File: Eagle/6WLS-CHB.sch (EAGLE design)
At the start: 26 parts, among them U1 DCDCCHB7505, U2 DCDCCHB7515, U3 DCDCCHB7515

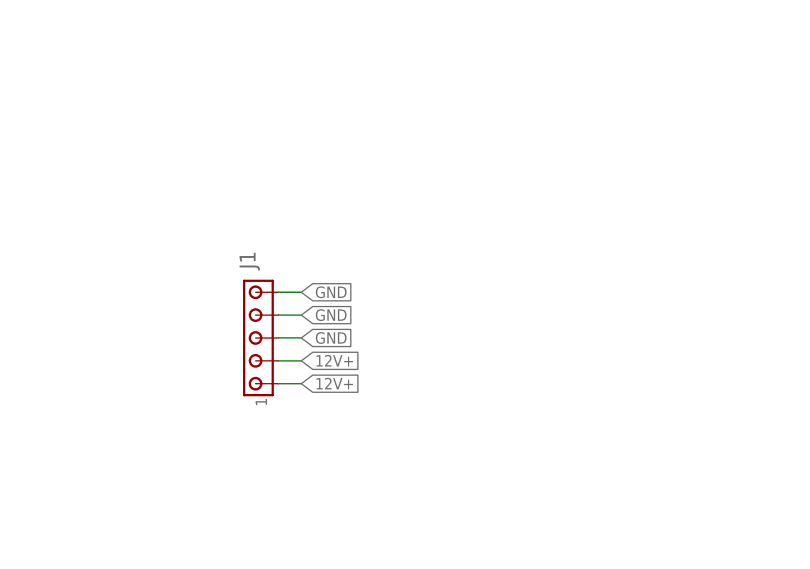
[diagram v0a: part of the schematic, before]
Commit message: Bigger terminal block.
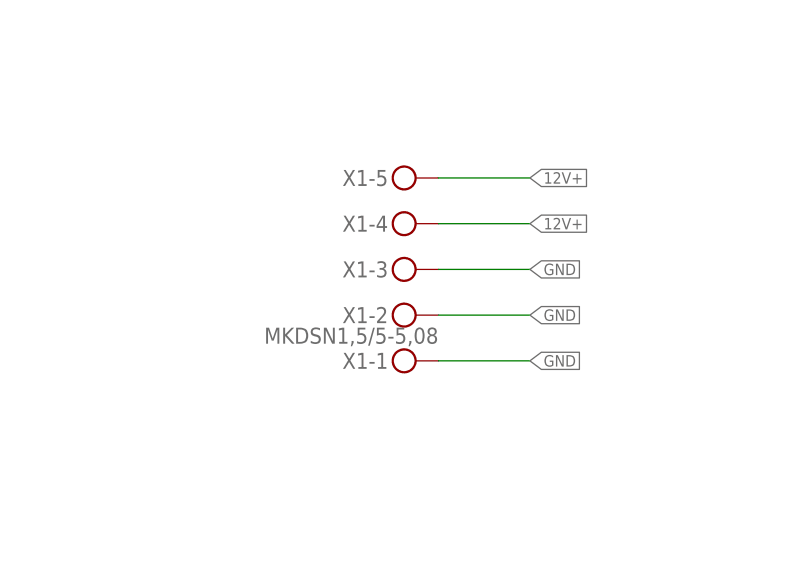
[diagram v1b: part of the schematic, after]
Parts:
- removed J1: (no value), con-amp:MTA05-156
- added X1: MKDSN1,5/5-5,08, con-phoenix-508:MKDSN1,5/5-5,08
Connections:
- net 12V+: now also X1-4.KL, X1-5.KL
- net GND: now also X1-1.KL, X1-2.KL, X1-3.KL
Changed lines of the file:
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@@
 <part name="U3" library="studio_h" deviceset="DCDC" device="CHB7515" value="DCDCCHB7515"/>
 <part name="H15" library="holes" deviceset="MOUNT-PAD-ROUND" device="3.3"/>
-<part name="J1" library="con-amp" deviceset="MTA05-156" device=""/>
+<part name="X1" library="con-phoenix-508" deviceset="MKDSN1,5/5-5,08" device=""/>
 </parts>
 <sheets>
@@
 <instance part="U3" gate="G$1" x="93.98" y="71.12"/>
 <instance part="H15" gate="G$1" x="274.32" y="93.98"/>
-<instance part="J1" gate="G$1" x="58.42" y="195.58" rot="R90"/>
+<instance part="X1" gate="-1" x="76.2" y="198.12" rot="R180"/>
+<instance part="X1" gate="-2" x="76.2" y="203.2" rot="R180"/>
+<instance part="X1" gate="-3" x="76.2" y="208.28" rot="R180"/>
+<instance part="X1" gate="-4" x="76.2" y="213.36" rot="R180"/>
+<instance part="X1" gate="-5" x="76.2" y="218.44" rot="R180"/>
 </instances>
 <busses>
@@
 </segment>
 <segment>
-<wire x1="60.96" y1="198.12" x2="63.5" y2="198.12" width="0.1524" layer="91"/>
-<label x="63.5" y="195.58" size="1.27" layer="95" font="vector" ratio="12" xref="yes"/>
-<label x="63.5" y="198.12" size="1.27" layer="95" font="vector" ratio="12" xref="yes"/>
-</segment>
-<segment>
-<wire x1="60.96" y1="195.58" x2="63.5" y2="195.58" width="0.1524" layer="91"/>
+<wire x1="78.74" y1="218.44" x2="88.9" y2="218.44" width="0.1524" layer="91"/>
+<label x="88.9" y="218.44" size="1.27" layer="95" font="vector" ratio="12" xref="yes"/>
+<pinref part="X1" gate="-5" pin="KL"/>
+</segment>
+<segment>
+<wire x1="78.74" y1="213.36" x2="88.9" y2="213.36" width="0.1524" layer="91"/>
+<label x="88.9" y="213.36" size="1.27" layer="95" font="vector" ratio="12" xref="yes"/>
+<pinref part="X1" gate="-4" pin="KL"/>
 </segment>
 </net>
@@
 </segment>
 <segment>
-<wire x1="60.96" y1="200.66" x2="63.5" y2="200.66" width="0.1524" layer="91"/>
-<label x="63.5" y="200.66" size="1.27" layer="95" font="vector" ratio="12" xref="yes"/>
-</segment>
-<segment>
-<wire x1="60.96" y1="203.2" x2="63.5" y2="203.2" width="0.1524" layer="91"/>
-<label x="63.5" y="203.2" size="1.27" layer="95" font="vector" ratio="12" xref="yes"/>
-</segment>
-<segment>
-<wire x1="60.96" y1="205.74" x2="63.5" y2="205.74" width="0.1524" layer="91"/>
-<label x="63.5" y="205.74" size="1.27" layer="95" font="vector" ratio="12" xref="yes"/>
-</segment>
-</net>
+<wire x1="78.74" y1="208.28" x2="88.9" y2="208.28" width="0.1524" layer="91"/>
+<label x="88.9" y="208.28" size="1.27" layer="95" font="vector" ratio="12" xref="yes"/>
+<pinref part="X1" gate="-3" pin="KL"/>
+</segment>
+<segment>
+<wire x1="78.74" y1="203.2" x2="88.9" y2="203.2" width="0.1524" layer="91"/>
+<label x="88.9" y="203.2" size="1.27" layer="95" font="vector" ratio="12" xref="yes"/>
+<pinref part="X1" gate="-2" pin="KL"/>
+</segment>
+<segment>
+<wire x1="78.74" y1="198.12" x2="88.9" y2="198.12" width="0.1524" layer="91"/>
+<label x="88.9" y="198.12" size="1.27" layer="95" font="vector" ratio="12" xref="yes"/>
+<pinref part="X1" gate="-1" pin="KL"/>
+</segment>
+</net>
